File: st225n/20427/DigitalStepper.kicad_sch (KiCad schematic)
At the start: 84 parts, among them J3 POWER, J6 STEPPER, Q10 DNI, U10 MC3479, U13 74F08, U14 74LS14, U15 74F38, U16 74F38, U17 74F38, U18 74F38, U2 74LS373, U20 7406, U21 11647-501, U23 74LS196, U24 74F74, U25 74F04, U26 74LS00, U29 74LS123, U3 CDM6264, U30 74F74, U31 74F109, U4 74LS373, X1 20MHz

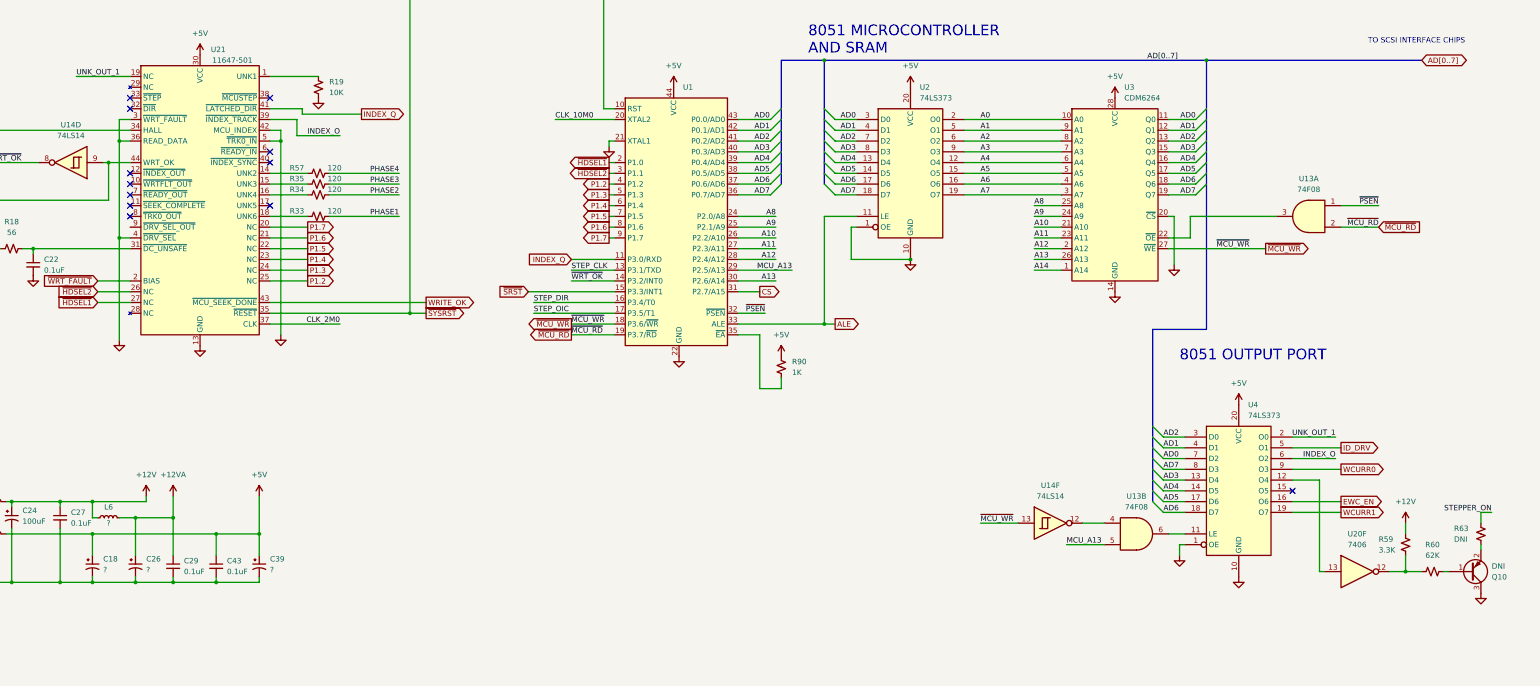
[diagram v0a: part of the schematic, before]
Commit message: Add component values. SRAM tweak.
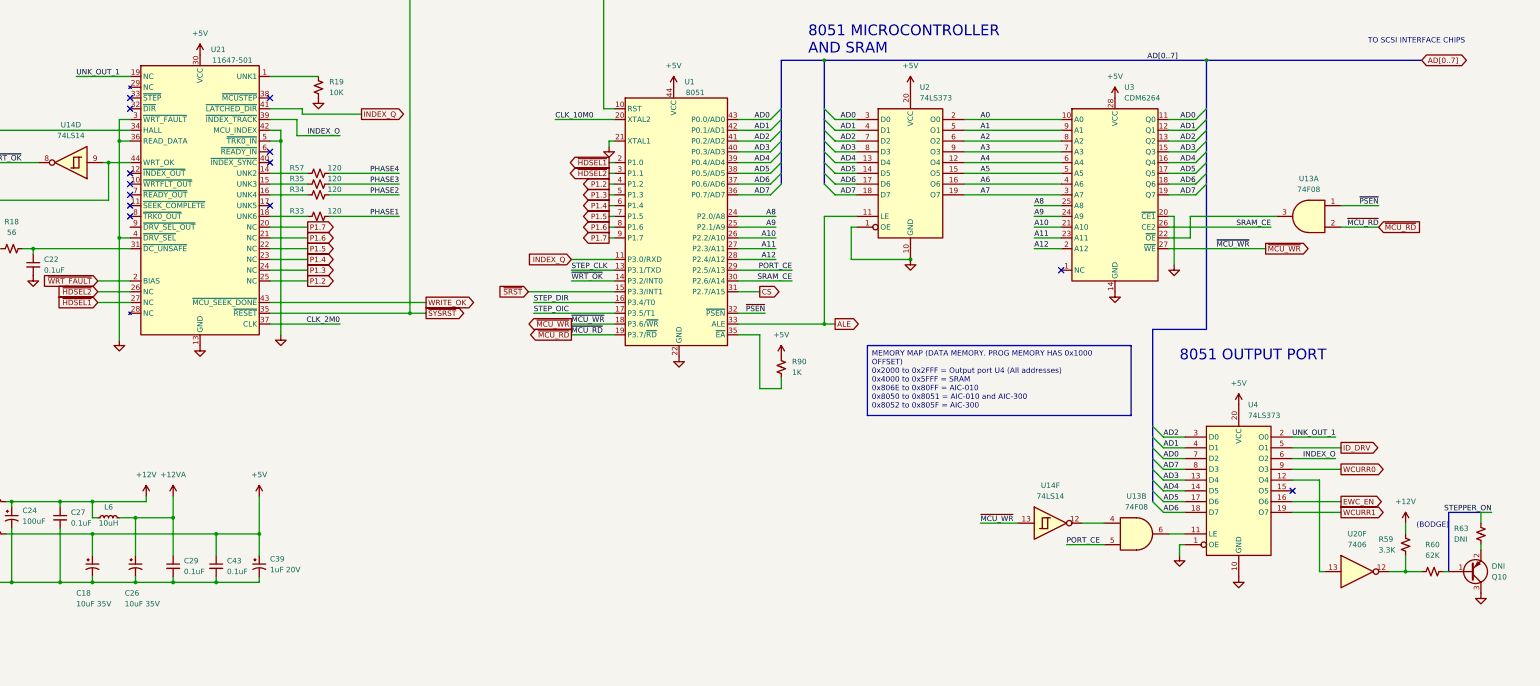
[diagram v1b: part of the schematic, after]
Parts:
- removed U3: CDM6264, Active:SOP127P1270X305-28_SHRINK, symbol Memory_RAM:KM62256CLP
- added U3: CDM6264, Active:SOP127P1270X305-28_SHRINK, symbol st225:SRAM_6264
- C18, C26: value ? -> 10uF 35V
- C39: value ? -> 1uF 20V
- L6: value ? -> 10uH
- U1: value ~ -> 8051
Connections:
- net +5V: now also U3.28 (VCC)
- net A0: now also U3.10 (A0)
- net A1: now also U3.9 (A1)
- net A10: now also U3.21 (A10)
- net A11: now also U3.23 (A11)
- net A12: now also U3.2 (A12)
- net A2: now also U3.8 (A2)
- net A3: now also U3.7 (A3)
- net A4: now also U3.6 (A4)
- net A5: now also U3.5 (A5)
- net A6: now also U3.4 (A6)
- net A7: now also U3.3 (A7)
- net A8: now also U3.25 (A8)
- net A9: now also U3.24 (A9)
- net AD0: now also U3.11 (Q0)
- net AD1: now also U3.12 (Q1)
- net AD2: now also U3.13 (Q2)
- net AD3: now also U3.15 (Q3)
- net AD4: now also U3.16 (Q4)
- net AD5: now also U3.17 (Q5)
- net AD6: now also U3.18 (Q6)
- net AD7: now also U3.19 (Q7)
- net GND: now also U3.14 (GND), U3.20 (~{CE1})
- net ~{MCU_WR}: now also U3.27 (~{WE})
- net at U13.3: now also U3.22 (~{OE})
- net A13 renamed SRAM_CE
- net SRAM_CE: now also U3.26 (CE2)
- net MCU_A13 renamed PORT_CE
- no-connect marks 20 -> 21
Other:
- note added: "(BODGE)"
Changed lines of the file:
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@@
   (no_connect (at 44.45 40.64))
   (no_connect (at 63.5 101.6))
+  (no_connect (at 283.21 142.24))
   (no_connect (at 44.45 33.02))
   (bus_entry (at 314.96 111.76) (size 2.54 -2.54)
@@
     (stroke (width 0) (type default))
   )
+  (wire (pts (xy 308.61 132.08) (xy 332.74 132.08))
+    (stroke (width 0) (type default))
+  )
   (wire (pts (xy 104.14 105.41) (xy 118.11 105.41))
     (stroke (width 0) (type default))
@@
     (stroke (width 0) (type default))
   )
+  (polyline (pts (xy 374.65 213.36) (xy 374.65 199.39))
+    (stroke (width 0) (type default) (color 255 0 255 1))
+  )
   (wire (pts (xy 99.06 111.76) (xy 99.06 157.48))
     (stroke (width 0) (type default))
@@
     (stroke (width 0) (type default))
   )
-  (wire (pts (xy 276.86 142.24) (xy 283.21 142.24))
-    (stroke (width 0) (type default))
-  )
   (wire (pts (xy 26.67 280.67) (xy 39.37 280.67))
     (stroke (width 0) (type default))
@@
     (stroke (width 0) (type default))
   )
-  (wire (pts (xy 207.01 144.78) (xy 215.9 144.78))
+  (wire (pts (xy 207.01 144.78) (xy 219.71 144.78))
     (stroke (width 0) (type default))
   )
@@
     (stroke (width 0) (type default))
   )
-  (wire (pts (xy 276.86 139.7) (xy 283.21 139.7))
-    (stroke (width 0) (type default))
-  )
   (wire (pts (xy 261.62 38.1) (xy 261.62 43.18))
     (stroke (width 0) (type default))
@@
     (stroke (width 0) (type default))
   )
+  (polyline (pts (xy 374.65 199.39) (xy 382.27 199.39))
+    (stroke (width 0) (type default) (color 255 0 255 1))
+  )
   (wire (pts (xy 199.39 248.92) (xy 209.55 248.92))
     (stroke (width 0) (type default))
@@
     (stroke (width 0) (type default))
   )
+  (text_box "MEMORY MAP (DATA MEMORY. PROG MEMORY HAS 0x1000 OFFSET)\n0x2000 to 0x2FFF = Output port U4 (All addresses)\n0x4000 to 0x5FFF = SRAM\n0x806E to 0x80FF = AIC-010\n0x8050 to 0x8051 = AIC-010 and AIC-300\n0x8052 to 0x805F = AIC-300"
+    (at 237.49 160.02 0) (size 62.23 16.51)
+    (stroke (width 0) (type default))
+    (fill (type none))
+    (effects (font (size 1.27 1.27)) (justify left top))
+  )
   (text "This work is licensed under a Creative Commons\nAttribution-ShareAlike 4.0 International License.\nSee https://creativecommons.org/licenses/by-sa/4.0/.\n"
     (at 242.57 283.21 0)
@@
     (effects (font (size 2.54 2.54)) (justify left bottom))
   )
+  (text "(BODGE)" (at 367.03 203.2 0)
+    (effects (font (size 1.27 1.27)) (justify left bottom))
+  )
   (text "TO SCSI INTERFACE CHIPS" (at 355.6 88.9 0)
     (effects (font (size 1.27 1.27)) (justify left bottom))
@@
     (effects (font (size 1.27 1.27)) (justify right bottom))
   )
-  (label "A14" (at 276.86 142.24 0) (fields_autoplaced)
-    (effects (font (size 1.27 1.27)) (justify left bottom))
-  )
   (label "~{WRT_OK}" (at 30.48 116.84 0) (fields_autoplaced)
     (effects (font (size 1.27 1.27)) (justify left bottom))
@@
     (effects (font (size 1.27 1.27)) (justify right bottom))
   )
-  (label "A13" (at 215.9 144.78 180) (fields_autoplaced)
+  (label "SRAM_CE" (at 219.71 144.78 180) (fields_autoplaced)
     (effects (font (size 1.27 1.27)) (justify right bottom))
   )
@@
     (effects (font (size 1.27 1.27)) (justify left bottom))
   )
-  (label "MCU_A13" (at 219.71 142.24 180) (fields_autoplaced)
+  (label "PORT_CE" (at 219.71 142.24 180) (fields_autoplaced)
     (effects (font (size 1.27 1.27)) (justify right bottom))
   )
@@
     (effects (font (size 1.27 1.27)) (justify left bottom))
   )
-  (label "A13" (at 276.86 139.7 0) (fields_autoplaced)
-    (effects (font (size 1.27 1.27)) (justify left bottom))
-  )
   (label "AD2" (at 210.82 111.76 0) (fields_autoplaced)
     (effects (font (size 1.27 1.27)) (justify left bottom))
@@
     (effects (font (size 1.27 1.27)) (justify right bottom))
   )
-  (label "MCU_A13" (at 284.48 207.01 0) (fields_autoplaced)
+  (label "PORT_CE" (at 284.48 207.01 0) (fields_autoplaced)
     (effects (font (size 1.27 1.27)) (justify left bottom))
   )
@@
     (effects (font (size 1.27 1.27)) (justify left bottom))
   )
+  (label "SRAM_CE" (at 332.74 132.08 180) (fields_autoplaced)
+    (effects (font (size 1.27 1.27)) (justify right bottom))
+  )
   (label "INDEX_O" (at 113.03 110.49 180) (fields_autoplaced)
     (effects (font (size 1.27 1.27)) (justify right bottom))
@@
     )
   )
-  (symbol (lib_id "Memory_RAM:KM62256CLP") (at 295.91 124.46 0) (unit 1)
-    (in_bom yes) (on_board yes) (dnp no) (fields_autoplaced)
-    (property "Reference" "U3" (at 298.1041 99.06 0)
-      (effects (font (size 1.27 1.27)) (justify left))
-    )
-    (property "Value" "CDM6264" (at 298.1041 101.6 0)
-      (effects (font (size 1.27 1.27)) (justify left))
-    )
-    (property "Footprint" "Active:SOP127P1270X305-28_SHRINK" (at 295.91 127 0)
-      (effects (font (size 1.27 1.27)) hide)
-    )
-    (property "Datasheet" "https://www.futurlec.com/Datasheet/Memory/62256.pdf" (at 295.91 127 0)
-      (effects (font (size 1.27 1.27)) hide)
-    )
-    (pin "14")
-    (pin "28")
-    (pin "1")
-    (pin "10")
-    (pin "11")
-    (pin "12")
-    (pin "13")
-    (pin "15")
-    (pin "16")
-    (pin "17")
-    (pin "18")
-    (pin "19")
-    (pin "2")
-    (pin "20")
-    (pin "21")
-    (pin "22")
-    (pin "23")
-    (pin "24")
-    (pin "25")
-    (pin "26")
-    (pin "27")
-    (pin "3")
-    (pin "4")
-    (pin "5")
-    (pin "6")
-    (pin "7")
-    (pin "8")
-    (pin "9")
-    (instances
-      (project "st225_20427"
-        (path "/ab051101-9873-4946-8bd3-ad87d2c27dee/dbd0d083-2822-4cc9-a670-4535f72ba9e6"
-          (reference "U3") (unit 1)
-        )
-      )
-    )
-  )
   (symbol (lib_id "st225:8051") (at 180.34 101.6 0) (unit 1)
-    (in_bom yes) (on_board yes) (dnp no) (fields_autoplaced)
-    (property "Reference" "U1" (at 193.9641 99.06 0)
+    (in_bom yes) (on_board yes) (dnp no)
+    (property "Reference" "U1" (at 194.31 97.79 0)
       (effects (font (size 1.27 1.27)) (justify left))
     )
-    (property "Value" "~" (at 180.34 101.6 0)
+    (property "Value" "8051" (at 196.85 100.33 0)
       (effects (font (size 1.27 1.27)))
     )
@@
       (effects (font (size 1.27 1.27)) (justify left))
     )
-    (property "Value" "?" (at 96.52 212.9282 0)
+    (property "Value" "1uF 20V" (at 96.52 212.9282 0)
       (effects (font (size 1.27 1.27)) (justify left))
     )
@@
   )
   (symbol (lib_id "Device:C_Polarized_Small_US") (at 64.77 212.09 0) (unit 1)
-    (in_bom yes) (on_board yes) (dnp no) (fields_autoplaced)
-    (property "Reference" "C26" (at 67.31 210.3882 0)
+    (in_bom yes) (on_board yes) (dnp no)
+    (property "Reference" "C26" (at 62.23 218.44 0)
       (effects (font (size 1.27 1.27)) (justify left))
     )
-    (property "Value" "?" (at 67.31 212.9282 0)
+    (property "Value" "10uF 35V" (at 62.23 220.98 0)
       (effects (font (size 1.27 1.27)) (justify left))
     )
@@
     )
   )
+  (symbol (lib_id "st225:SRAM_6264") (at 295.91 124.46 0) (unit 1)
+    (in_bom yes) (on_board yes) (dnp no) (fields_autoplaced)
+    (property "Reference" "U3" (at 298.1041 99.06 0)
+      (effects (font (size 1.27 1.27)) (justify left))
+    )
+    (property "Value" "CDM6264" (at 298.1041 101.6 0)
+      (effects (font (size 1.27 1.27)) (justify left))
+    )
+    (property "Footprint" "Active:SOP127P1270X305-28_SHRINK" (at 295.91 124.46 0)
+      (effects (font (size 1.27 1.27)) hide)
+    )
+    (property "Datasheet" "" (at 295.91 124.46 0)
+      (effects (font (size 1.27 1.27)) hide)
+    )
+    (pin "14")
+    (pin "28")
+    (pin "1")
+    (pin "10")
+    (pin "11")
+    (pin "12")
+    (pin "13")
+    (pin "15")
+    (pin "16")
+    (pin "17")
+    (pin "18")
+    (pin "19")
+    (pin "2")
+    (pin "20")
+    (pin "21")
+    (pin "22")
+    (pin "23")
+    (pin "24")
+    (pin "25")
+    (pin "26")
+    (pin "27")
+    (pin "3")
+    (pin "4")
+    (pin "5")
+    (pin "6")
+    (pin "7")
+    (pin "8")
+    (pin "9")
+    (instances
+      (project "st225_20427"
+        (path "/ab051101-9873-4946-8bd3-ad87d2c27dee/dbd0d083-2822-4cc9-a670-4535f72ba9e6"
+          (reference "U3") (unit 1)
+        )
+      )
+    )
+  )
   (symbol (lib_id "74xx:74LS74") (at 52.07 266.7 0) (unit 3)
     (in_bom yes) (on_board yes) (dnp no)
@@
   )
   (symbol (lib_id "Device:C_Polarized_Small_US") (at 54.61 212.09 0) (unit 1)
-    (in_bom yes) (on_board yes) (dnp no) (fields_autoplaced)
-    (property "Reference" "C18" (at 57.15 210.3882 0)
+    (in_bom yes) (on_board yes) (dnp no)
+    (property "Reference" "C18" (at 50.8 218.44 0)
       (effects (font (size 1.27 1.27)) (justify left))
     )
-    (property "Value" "?" (at 57.15 212.9282 0)
+    (property "Value" "10uF 35V" (at 50.8 220.98 0)
       (effects (font (size 1.27 1.27)) (justify left))
     )
@@
       (effects (font (size 1.27 1.27)))
     )
-    (property "Value" "?" (at 58.42 201.93 90)
+    (property "Value" "10uH" (at 58.42 201.93 90)
       (effects (font (size 1.27 1.27)))
     )
